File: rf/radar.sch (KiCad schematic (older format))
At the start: 13 parts, among them J102 Conn_01x01, J103 Conn_01x01, J106 Conn_01x02, J108 Conn_Coaxial, J109 Conn_Coaxial

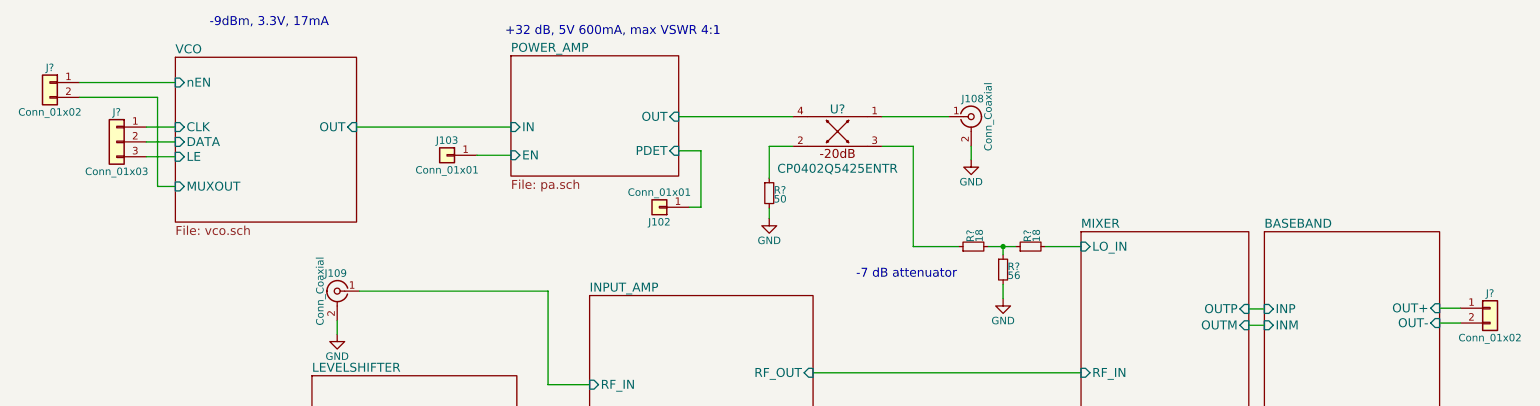
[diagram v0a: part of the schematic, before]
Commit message: Finish assigning component footprints
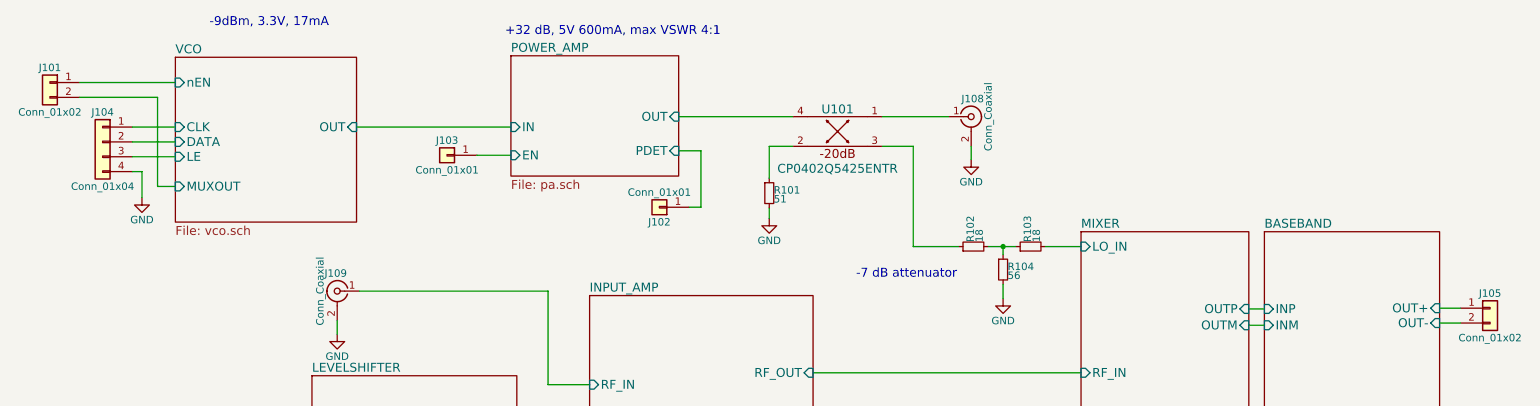
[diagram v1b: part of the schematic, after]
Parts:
- removed J?: Conn_01x03, symbol Conn_01x03
- added J104: Conn_01x04, Socket_Strips:Socket_Strip_Straight_1x04_Pitch2.54mm, symbol Conn_01x04
- J101, J105: renamed from J?; footprint (none) -> Pin_Headers:Pin_Header_Straight_1x02_Pitch2.54mm
- R101: renamed from R?; value 50 -> 51; footprint (none) -> Resistors_SMD:R_0402
- R102, R103, R104: renamed from R?; footprint (none) -> Resistors_SMD:R_0402
- U101: renamed from U?; footprint (none) -> rajsradar:CP0402
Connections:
- net GND: now also J104.4 (Pin_4)
- net VCO/CLK: now also J104.1 (Pin_1)
- net VCO/DATA: now also J104.2 (Pin_2)
- net VCO/LE: now also J104.3 (Pin_3)
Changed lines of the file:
@@
 $EndComp
 $Comp
-L GND #PWR025
+L GND #PWR105
 U 1 1 5A5A8BA4
 P 2785 3045
-F 0 "#PWR025" H 2785 2795 50  0001 C CNN
+F 0 "#PWR105" H 2785 2795 50  0001 C CNN
 F 1 "GND" H 2785 2895 50  0000 C CNN
 F 2 "" H 2785 3045 50  0001 C CNN
@@
 	2785 2955 2785 3045
 $Comp
-L GND #PWR?
+L GND #PWR101
 U 1 1 5A81DCC1
 P 7055 1870
-F 0 "#PWR?" H 7055 1620 50  0001 C CNN
+F 0 "#PWR101" H 7055 1620 50  0001 C CNN
 F 1 "GND" H 7055 1720 50  0000 C CNN
 F 2 "" H 7055 1870 50  0001 C CNN
@@
 	7055 1780 7055 1870
 $Comp
-L R_Small R?
+L R_Small R101
 U 1 1 5AB9E28B
 P 5695 2095
-F 0 "R?" H 5725 2115 50  0000 L CNN
-F 1 "50" H 5725 2055 50  0000 L CNN
-F 2 "" H 5695 2095 50  0001 C CNN
+F 0 "R101" H 5725 2115 50  0000 L CNN
+F 1 "51" H 5725 2055 50  0000 L CNN
+F 2 "Resistors_SMD:R_0402" H 5695 2095 50  0001 C CNN
 F 3 "" H 5695 2095 50  0001 C CNN
 	1    5695 2095
@@
 	5695 1780 5855 1780
 $Comp
-L GND #PWR?
+L GND #PWR103
 U 1 1 5AB9E91D
 P 5695 2265
-F 0 "#PWR?" H 5695 2015 50  0001 C CNN
+F 0 "#PWR103" H 5695 2015 50  0001 C CNN
 F 1 "GND" H 5695 2115 50  0000 C CNN
 F 2 "" H 5695 2265 50  0001 C CNN
@@
 	8925 2985 9030 2985
 $Comp
-L R_Small R?
+L R_Small R102
 U 1 1 5ABA127F
 P 7070 2455
-F 0 "R?" H 7100 2475 50  0000 L CNN
+F 0 "R102" H 7100 2475 50  0000 L CNN
 F 1 "18" H 7100 2415 50  0000 L CNN
-F 2 "" H 7070 2455 50  0001 C CNN
+F 2 "Resistors_SMD:R_0402" H 7070 2455 50  0001 C CNN
 F 3 "" H 7070 2455 50  0001 C CNN
 	1    7070 2455
@@
 $EndComp
 $Comp
-L R_Small R?
+L R_Small R104
 U 1 1 5ABA1386
 P 7270 2610
-F 0 "R?" H 7300 2630 50  0000 L CNN
+F 0 "R104" H 7300 2630 50  0000 L CNN
 F 1 "56" H 7300 2570 50  0000 L CNN
-F 2 "" H 7270 2610 50  0001 C CNN
+F 2 "Resistors_SMD:R_0402" H 7270 2610 50  0001 C CNN
 F 3 "" H 7270 2610 50  0001 C CNN
 	1    7270 2610
@@
 $EndComp
 $Comp
-L GND #PWR?
+L GND #PWR104
 U 1 1 5ABA147B
 P 7270 2805
-F 0 "#PWR?" H 7270 2555 50  0001 C CNN
+F 0 "#PWR104" H 7270 2555 50  0001 C CNN
 F 1 "GND" H 7270 2655 50  0000 C CNN
 F 2 "" H 7270 2805 50  0001 C CNN
@@
 	7270 2805 7270 2710
 $Comp
-L R_Small R?
+L R_Small R103
 U 1 1 5ABA17C3
 P 7455 2455
-F 0 "R?" H 7485 2475 50  0000 L CNN
+F 0 "R103" H 7485 2475 50  0000 L CNN
 F 1 "18" H 7485 2415 50  0000 L CNN
-F 2 "" H 7455 2455 50  0001 C CNN
+F 2 "Resistors_SMD:R_0402" H 7455 2455 50  0001 C CNN
 F 3 "" H 7455 2455 50  0001 C CNN
 	1    7455 2455
@@
 -7 dB attenuator
 $Comp
-L CP0402Q5425ENTR U?
+L CP0402Q5425ENTR U101
 U 1 1 5AB92165
 P 6155 1680
-F 0 "U?" H 6155 1830 60  0000 C CNN
+F 0 "U101" H 6155 1830 60  0000 C CNN
 F 1 "CP0402Q5425ENTR" H 6155 1430 60  0000 C CNN
-F 2 "" H 6155 1730 60  0001 C CNN
+F 2 "rajsradar:CP0402" H 6155 1730 60  0001 C CNN
 F 3 "" H 6155 1730 60  0001 C CNN
 	1    6155 1680
 	1    0    0    -1
 $EndComp
-$Comp
-L Conn_01x03 J?
-U 1 1 5AB9811C
-P 1300 1750
-F 0 "J?" H 1300 1950 50  0000 C CNN
-F 1 "Conn_01x03" H 1300 1550 50  0000 C CNN
-F 2 "" H 1300 1750 50  0001 C CNN
-F 3 "" H 1300 1750 50  0001 C CNN
-	1    1300 1750
-	-1   0    0    -1
-$EndComp
-Wire Wire Line
-	1500 1650 1695 1650
-Wire Wire Line
-	1695 1750 1500 1750
-Wire Wire Line
-	1500 1850 1695 1850
-$Comp
-L Conn_01x02 J?
+Wire Wire Line
+	1405 1650 1695 1650
+Wire Wire Line
+	1405 1750 1695 1750
+Wire Wire Line
+	1405 1850 1695 1850
+$Comp
+L Conn_01x02 J101
 U 1 1 5AB988B6
 P 850 1350
-F 0 "J?" H 850 1450 50  0000 C CNN
+F 0 "J101" H 850 1450 50  0000 C CNN
 F 1 "Conn_01x02" H 850 1150 50  0000 C CNN
-F 2 "" H 850 1350 50  0001 C CNN
+F 2 "Pin_Headers:Pin_Header_Straight_1x02_Pitch2.54mm" H 850 1350 50  0001 C CNN
 F 3 "" H 850 1350 50  0001 C CNN
 	1    850  1350
@@
 	1575 2050 1695 2050
 $Comp
-L Conn_01x02 J?
+L Conn_01x02 J105
 U 1 1 5AC395BB
 P 10550 2870
-F 0 "J?" H 10550 2970 50  0000 C CNN
+F 0 "J105" H 10550 2970 50  0000 C CNN
 F 1 "Conn_01x02" H 10550 2670 50  0000 C CNN
-F 2 "" H 10550 2870 50  0001 C CNN
+F 2 "Pin_Headers:Pin_Header_Straight_1x02_Pitch2.54mm" H 10550 2870 50  0001 C CNN
 F 3 "" H 10550 2870 50  0001 C CNN
 	1    10550 2870
@@
 Wire Wire Line
 	5990 3305 7795 3305
+$Comp
+L Conn_01x04 J104
+U 1 1 5AC9D699
+P 1205 1750
+F 0 "J104" H 1205 1950 50  0000 C CNN
+F 1 "Conn_01x04" H 1205 1450 50  0000 C CNN
+F 2 "Socket_Strips:Socket_Strip_Straight_1x04_Pitch2.54mm" H 1205 1750 50  0001 C CNN
+F 3 "" H 1205 1750 50  0001 C CNN
+	1    1205 1750
+	-1   0    0    -1
+$EndComp
+$Comp
+L GND #PWR102
+U 1 1 5AC9DE90
+P 1470 2125
+F 0 "#PWR102" H 1470 1875 50  0001 C CNN
+F 1 "GND" H 1470 1975 50  0000 C CNN
+F 2 "" H 1470 2125 50  0001 C CNN
+F 3 "" H 1470 2125 50  0001 C CNN
+	1    1470 2125
+	1    0    0    -1
+$EndComp
+Wire Wire Line
+	1470 2125 1470 1950
+Wire Wire Line
+	1470 1950 1405 1950
 $EndSCHEMATC

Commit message: Finish first revision layout
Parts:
- J104: renamed from J103; footprint Connectors:1pin -> Socket_Strips:Socket_Strip_Straight_1x01_Pitch2.54mm
- J105: renamed from J102; footprint Connectors:1pin -> Socket_Strips:Socket_Strip_Straight_1x01_Pitch2.54mm
- renumbered J108 to J102, J104 to J103, J109 to J106, J105 to J107, J106 to J108
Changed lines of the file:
@@
 LIBS:mc2016k30
 LIBS:cp0402q5425entr
+LIBS:lm340-5
 EELAYER 25 0
 EELAYER END
@@
 	3995 3765 4485 3765
 $Comp
-L Conn_01x02 J106
+L Conn_01x02 J108
 U 1 1 5A51B599
 P 2205 3665
-F 0 "J106" H 2205 3765 50  0000 C CNN
+F 0 "J108" H 2205 3765 50  0000 C CNN
 F 1 "Conn_01x02" H 2205 3465 50  0000 C CNN
 F 2 "Socket_Strips:Socket_Strip_Straight_1x02_Pitch2.54mm" H 2205 3665 50  0001 C CNN
@@
 	2405 3765 2615 3765
 $Comp
-L Conn_01x01 J103
+L Conn_01x01 J104
 U 1 1 5A511684
 P 3525 1840
-F 0 "J103" H 3525 1940 50  0000 C CNN
+F 0 "J104" H 3525 1940 50  0000 C CNN
 F 1 "Conn_01x01" H 3525 1740 50  0000 C CNN
-F 2 "Connectors:1pin" H 3525 1840 50  0001 C CNN
+F 2 "Socket_Strips:Socket_Strip_Straight_1x01_Pitch2.54mm" H 3525 1840 50  0001 C CNN
 F 3 "" H 3525 1840 50  0001 C CNN
 	1    3525 1840
@@
 	3725 1840 3955 1840
 $Comp
-L Conn_01x01 J102
+L Conn_01x01 J105
 U 1 1 5A5123F2
 P 4955 2190
-F 0 "J102" H 4955 2290 50  0000 C CNN
+F 0 "J105" H 4955 2290 50  0000 C CNN
 F 1 "Conn_01x01" H 4955 2090 50  0000 C CNN
-F 2 "Connectors:1pin" H 4955 2190 50  0001 C CNN
+F 2 "Socket_Strips:Socket_Strip_Straight_1x01_Pitch2.54mm" H 4955 2190 50  0001 C CNN
 F 3 "" H 4955 2190 50  0001 C CNN
 	1    4955 2190
@@
 	5235 1810 5085 1810
 $Comp
-L Conn_Coaxial J109
+L Conn_Coaxial J106
 U 1 1 5A5A7286
 P 2785 2755
-F 0 "J109" H 2795 2875 50  0000 C CNN
+F 0 "J106" H 2795 2875 50  0000 C CNN
 F 1 "Conn_Coaxial" V 2900 2755 50  0000 C CNN
 F 2 "rajsradar:132322" H 2785 2755 50  0001 C CNN
@@
 $EndComp
 $Comp
-L Conn_Coaxial J108
+L Conn_Coaxial J102
 U 1 1 5A5A73C3
 P 7055 1580
-F 0 "J108" H 7065 1700 50  0000 C CNN
+F 0 "J102" H 7065 1700 50  0000 C CNN
 F 1 "Conn_Coaxial" V 7170 1580 50  0000 C CNN
 F 2 "rajsradar:132322" H 7055 1580 50  0001 C CNN
@@
 	1575 2050 1695 2050
 $Comp
-L Conn_01x02 J105
+L Conn_01x02 J107
 U 1 1 5AC395BB
 P 10550 2870
-F 0 "J105" H 10550 2970 50  0000 C CNN
+F 0 "J107" H 10550 2970 50  0000 C CNN
 F 1 "Conn_01x02" H 10550 2670 50  0000 C CNN
 F 2 "Pin_Headers:Pin_Header_Straight_1x02_Pitch2.54mm" H 10550 2870 50  0001 C CNN
@@
 	5990 3305 7795 3305
 $Comp
-L Conn_01x04 J104
+L Conn_01x04 J103
 U 1 1 5AC9D699
 P 1205 1750
-F 0 "J104" H 1205 1950 50  0000 C CNN
+F 0 "J103" H 1205 1950 50  0000 C CNN
 F 1 "Conn_01x04" H 1205 1450 50  0000 C CNN
 F 2 "Socket_Strips:Socket_Strip_Straight_1x04_Pitch2.54mm" H 1205 1750 50  0001 C CNN

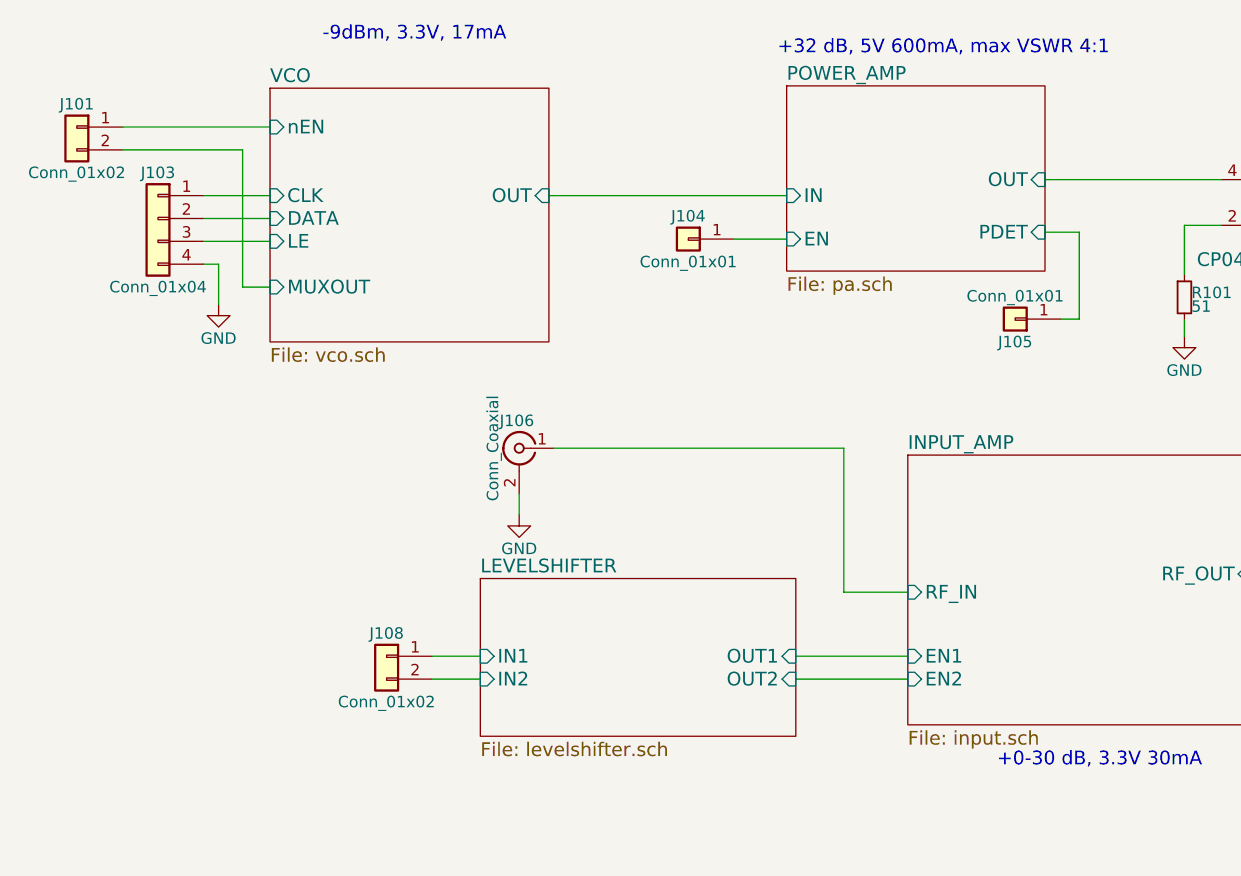
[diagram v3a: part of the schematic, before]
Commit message: Massage vias to improve planes and swap out connectors to get more ground lines
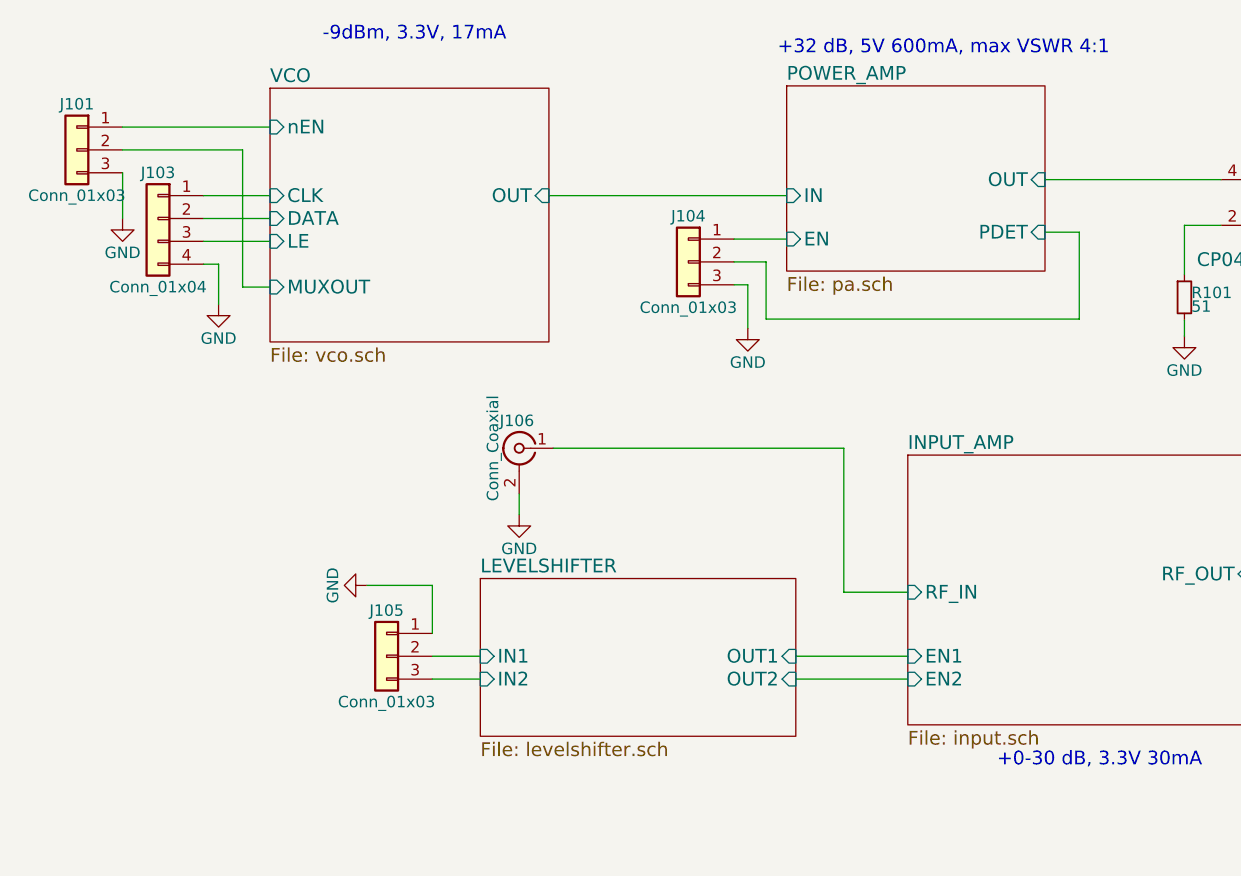
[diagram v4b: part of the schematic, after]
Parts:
- removed J101: Conn_01x02, Pin_Headers:Pin_Header_Straight_1x02_Pitch2.54mm, symbol Conn_01x02
- removed J104, J105: Conn_01x01, Socket_Strips:Socket_Strip_Straight_1x01_Pitch2.54mm, symbol Conn_01x01
- removed J108: Conn_01x02, Socket_Strips:Socket_Strip_Straight_1x02_Pitch2.54mm, symbol Conn_01x02
- added J101, J104, J105: Conn_01x03, Socket_Strips:Socket_Strip_Straight_1x03_Pitch2.54mm, symbol Conn_01x03
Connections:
- net GND: now also J101.3 (Pin_3), J104.3 (Pin_3), J105.1 (Pin_1)
- net LEVELSHIFTER/IN1: now also J105.2 (Pin_2)
- net LEVELSHIFTER/IN2: now also J105.3 (Pin_3)
- net POWER_AMP/EN: now also J104.1 (Pin_1)
- net POWER_AMP/PDET: now also J104.2 (Pin_2)
- net VCO/MUXOUT: now also J101.2 (Pin_2)
- net VCO/nEN: now also J101.1 (Pin_1)
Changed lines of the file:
@@
 Wire Wire Line
 	3995 3765 4485 3765
-$Comp
-L Conn_01x02 J108
-U 1 1 5A51B599
-P 2205 3665
-F 0 "J108" H 2205 3765 50  0000 C CNN
-F 1 "Conn_01x02" H 2205 3465 50  0000 C CNN
-F 2 "Socket_Strips:Socket_Strip_Straight_1x02_Pitch2.54mm" H 2205 3665 50  0001 C CNN
-F 3 "" H 2205 3665 50  0001 C CNN
-	1    2205 3665
-	-1   0    0    -1
-$EndComp
 Wire Wire Line
 	2405 3665 2615 3665
 Wire Wire Line
 	2405 3765 2615 3765
-$Comp
-L Conn_01x01 J104
-U 1 1 5A511684
-P 3525 1840
-F 0 "J104" H 3525 1940 50  0000 C CNN
-F 1 "Conn_01x01" H 3525 1740 50  0000 C CNN
-F 2 "Socket_Strips:Socket_Strip_Straight_1x01_Pitch2.54mm" H 3525 1840 50  0001 C CNN
-F 3 "" H 3525 1840 50  0001 C CNN
-	1    3525 1840
-	-1   0    0    -1
-$EndComp
 Wire Wire Line
 	3725 1840 3955 1840
-$Comp
-L Conn_01x01 J105
-U 1 1 5A5123F2
-P 4955 2190
-F 0 "J105" H 4955 2290 50  0000 C CNN
-F 1 "Conn_01x01" H 4955 2090 50  0000 C CNN
-F 2 "Socket_Strips:Socket_Strip_Straight_1x01_Pitch2.54mm" H 4955 2190 50  0001 C CNN
-F 3 "" H 4955 2190 50  0001 C CNN
-	1    4955 2190
-	-1   0    0    1
-$EndComp
 Wire Wire Line
 	5235 1810 5085 1810
@@
 $EndComp
 $Comp
-L GND #PWR01
+L GND #PWR107
 U 1 1 5A5A8BA4
 P 2785 3045
-F 0 "#PWR01" H 2785 2795 50  0001 C CNN
+F 0 "#PWR107" H 2785 2795 50  0001 C CNN
 F 1 "GND" H 2785 2895 50  0000 C CNN
 F 2 "" H 2785 3045 50  0001 C CNN
@@
 	2785 2955 2785 3045
 $Comp
-L GND #PWR02
+L GND #PWR102
 U 1 1 5A81DCC1
 P 7055 1870
-F 0 "#PWR02" H 7055 1620 50  0001 C CNN
+F 0 "#PWR102" H 7055 1620 50  0001 C CNN
 F 1 "GND" H 7055 1720 50  0000 C CNN
 F 2 "" H 7055 1870 50  0001 C CNN
@@
 $EndComp
 Wire Wire Line
-	5155 2190 5235 2190
+	3865 2190 5235 2190
 Wire Wire Line
 	5235 2190 5235 1810
@@
 	5695 1780 5855 1780
 $Comp
-L GND #PWR03
+L GND #PWR105
 U 1 1 5AB9E91D
 P 5695 2265
-F 0 "#PWR03" H 5695 2015 50  0001 C CNN
+F 0 "#PWR105" H 5695 2015 50  0001 C CNN
 F 1 "GND" H 5695 2115 50  0000 C CNN
 F 2 "" H 5695 2265 50  0001 C CNN
@@
 $EndComp
 $Comp
-L GND #PWR04
+L GND #PWR106
 U 1 1 5ABA147B
 P 7270 2805
-F 0 "#PWR04" H 7270 2555 50  0001 C CNN
+F 0 "#PWR106" H 7270 2555 50  0001 C CNN
 F 1 "GND" H 7270 2655 50  0000 C CNN
 F 2 "" H 7270 2805 50  0001 C CNN
@@
 Wire Wire Line
 	1405 1850 1695 1850
-$Comp
-L Conn_01x02 J101
-U 1 1 5AB988B6
-P 850 1350
-F 0 "J101" H 850 1450 50  0000 C CNN
-F 1 "Conn_01x02" H 850 1150 50  0000 C CNN
-F 2 "Pin_Headers:Pin_Header_Straight_1x02_Pitch2.54mm" H 850 1350 50  0001 C CNN
-F 3 "" H 850 1350 50  0001 C CNN
-	1    850  1350
-	-1   0    0    -1
-$EndComp
 Wire Wire Line
 	1050 1350 1695 1350
@@
 $EndComp
 $Comp
-L GND #PWR05
+L GND #PWR103
 U 1 1 5AC9DE90
 P 1470 2125
-F 0 "#PWR05" H 1470 1875 50  0001 C CNN
+F 0 "#PWR103" H 1470 1875 50  0001 C CNN
 F 1 "GND" H 1470 1975 50  0000 C CNN
 F 2 "" H 1470 2125 50  0001 C CNN
@@
 Wire Wire Line
 	1470 1950 1405 1950
+$Comp
+L Conn_01x03 J104
+U 1 1 5AD3D57C
+P 3525 1940
+F 0 "J104" H 3525 2140 50  0000 C CNN
+F 1 "Conn_01x03" H 3525 1740 50  0000 C CNN
+F 2 "Socket_Strips:Socket_Strip_Straight_1x03_Pitch2.54mm" H 3525 1940 50  0001 C CNN
+F 3 "" H 3525 1940 50  0001 C CNN
+	1    3525 1940
+	-1   0    0    -1
+$EndComp
+$Comp
+L Conn_01x03 J105
+U 1 1 5AD3D9FE
+P 2205 3665
+F 0 "J105" H 2205 3865 50  0000 C CNN
+F 1 "Conn_01x03" H 2205 3465 50  0000 C CNN
+F 2 "Socket_Strips:Socket_Strip_Straight_1x03_Pitch2.54mm" H 2205 3665 50  0001 C CNN
+F 3 "" H 2205 3665 50  0001 C CNN
+	1    2205 3665
+	-1   0    0    -1
+$EndComp
+$Comp
+L Conn_01x03 J101
+U 1 1 5AD3F40A
+P 850 1450
+F 0 "J101" H 850 1650 50  0000 C CNN
+F 1 "Conn_01x03" H 850 1250 50  0000 C CNN
+F 2 "Socket_Strips:Socket_Strip_Straight_1x03_Pitch2.54mm" H 850 1450 50  0001 C CNN
+F 3 "" H 850 1450 50  0001 C CNN
+	1    850  1450
+	-1   0    0    -1
+$EndComp
+$Comp
+L GND #PWR101
+U 1 1 5AD3FB7F
+P 1050 1750
+F 0 "#PWR101" H 1050 1500 50  0001 C CNN
+F 1 "GND" H 1050 1600 50  0000 C CNN
+F 2 "" H 1050 1750 50  0001 C CNN
+F 3 "" H 1050 1750 50  0001 C CNN
+	1    1050 1750
+	1    0    0    -1
+$EndComp
+Wire Wire Line
+	1050 1550 1050 1750
+$Comp
+L GND #PWR108
+U 1 1 5AD3FF1F
+P 2120 3355
+F 0 "#PWR108" H 2120 3105 50  0001 C CNN
+F 1 "GND" H 2120 3205 50  0000 C CNN
+F 2 "" H 2120 3355 50  0001 C CNN
+F 3 "" H 2120 3355 50  0001 C CNN
+	1    2120 3355
+	0    1    1    0
+$EndComp
+Wire Wire Line
+	2120 3355 2405 3355
+Wire Wire Line
+	3725 1940 3865 1940
+Wire Wire Line
+	3865 1940 3865 2190
+$Comp
+L GND #PWR104
+U 1 1 5AD421C5
+P 3785 2230
+F 0 "#PWR104" H 3785 1980 50  0001 C CNN
+F 1 "GND" H 3785 2080 50  0000 C CNN
+F 2 "" H 3785 2230 50  0001 C CNN
+F 3 "" H 3785 2230 50  0001 C CNN
+	1    3785 2230
+	1    0    0    -1
+$EndComp
+Wire Wire Line
+	3785 2230 3785 2040
+Wire Wire Line
+	3785 2040 3725 2040
+Wire Wire Line
+	2405 3355 2405 3565
 $EndSCHEMATC
